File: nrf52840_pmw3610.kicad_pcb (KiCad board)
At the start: 2 copper layers, 18 x 33 mm, 3 parts, among them J1 PMW3360_Connector, J2 Battery_JST-PH, U1 SuperMini_nRF52840

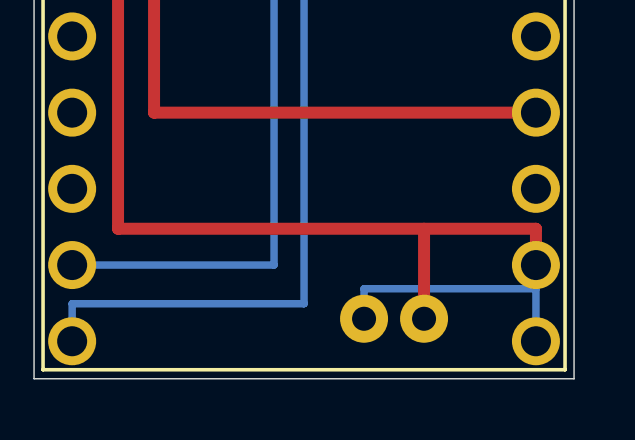
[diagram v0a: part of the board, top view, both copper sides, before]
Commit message: fix: BATINルートをy=30.5に変更してU1R pin23(GND)パッドとの短絡を解消
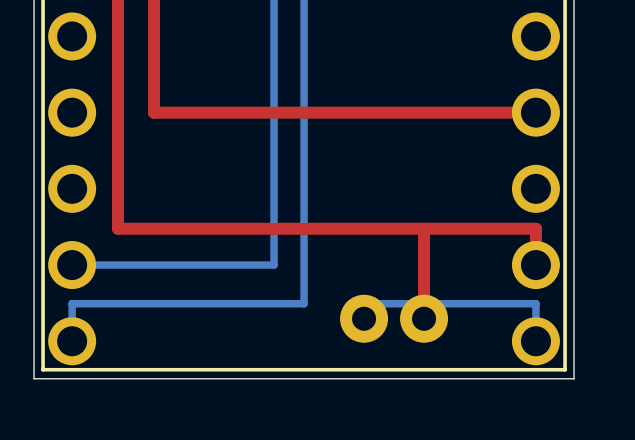
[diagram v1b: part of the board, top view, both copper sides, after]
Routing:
- net BATIN: track 8.48 -> 7.48 mm
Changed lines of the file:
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@@
 (segment (start 139.0000 86.2700) (end 139.0000 109.1300) (width 0.4000) (layer "F.Cu") (net 2))
 (segment (start 139.0000 109.1300) (end 151.7300 109.1300) (width 0.4000) (layer "F.Cu") (net 2))
-(segment (start 146.0000 116.0000) (end 146.0000 115.0000) (width 0.2500) (layer "B.Cu") (net 8))
-(segment (start 146.0000 115.0000) (end 151.7300 115.0000) (width 0.2500) (layer "B.Cu") (net 8))
-(segment (start 151.7300 115.0000) (end 151.7300 116.7500) (width 0.2500) (layer "B.Cu") (net 8))
+(segment (start 146.0000 116.0000) (end 146.0000 115.5000) (width 0.2500) (layer "B.Cu") (net 8))
+(segment (start 146.0000 115.5000) (end 151.7300 115.5000) (width 0.2500) (layer "B.Cu") (net 8))
+(segment (start 151.7300 115.5000) (end 151.7300 116.7500) (width 0.2500) (layer "B.Cu") (net 8))
 (segment (start 151.0000 86.2700) (end 150.1000 86.2700) (width 0.2500) (layer "B.Cu") (net 6))
 (segment (start 150.1000 86.2700) (end 150.1000 97.7000) (width 0.2500) (layer "B.Cu") (net 6))
